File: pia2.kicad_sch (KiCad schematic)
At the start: 40 parts, among them IC25 LM393P, IC31 74LS02N, IC34 MC14050BCP, IC35 MC6821

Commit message: handle 27C512
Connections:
- net GND: no longer IC35.12 (PB2)
- new net MEM-SIZE: IC35.12 (PB2)
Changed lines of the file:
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@@
     )
   )
-  (global_label "GM2" (shape input) (at 74.93 87.122 0) (fields_autoplaced)
-    (effects (font (size 1.27 1.27)) (justify left))
-    (property "Intersheetrefs" "${INTERSHEET_REFS}" (at 81.1852 87.0426 0)
-      (effects (font (size 1.27 1.27)) (justify left) hide)
-    )
-  )
-  (global_label "GM1" (shape input) (at 74.93 84.582 0) (fields_autoplaced)
-    (effects (font (size 1.27 1.27)) (justify left))
-    (property "Intersheetrefs" "${INTERSHEET_REFS}" (at 81.1852 84.5026 0)
+  (global_label "GM2" (shape output) (at 74.93 87.122 0) (fields_autoplaced)
+    (effects (font (size 1.27 1.27)) (justify left))
+    (property "Intersheetrefs" "${INTERSHEET_REFS}" (at 81.1125 87.122 0)
+      (effects (font (size 1.27 1.27)) (justify left) hide)
+    )
+  )
+  (global_label "GM1" (shape output) (at 74.93 84.582 0) (fields_autoplaced)
+    (effects (font (size 1.27 1.27)) (justify left))
+    (property "Intersheetrefs" "${INTERSHEET_REFS}" (at 81.1125 84.582 0)
       (effects (font (size 1.27 1.27)) (justify left) hide)
     )
@@
     )
   )
-  (global_label "GM0" (shape input) (at 74.93 82.042 0) (fields_autoplaced)
-    (effects (font (size 1.27 1.27)) (justify left))
-    (property "Intersheetrefs" "${INTERSHEET_REFS}" (at 81.1852 81.9626 0)
+  (global_label "GM0" (shape output) (at 74.93 82.042 0) (fields_autoplaced)
+    (effects (font (size 1.27 1.27)) (justify left))
+    (property "Intersheetrefs" "${INTERSHEET_REFS}" (at 81.1125 82.042 0)
       (effects (font (size 1.27 1.27)) (justify left) hide)
     )
@@
     )
   )
-  (global_label "CSS" (shape input) (at 74.93 79.502 0) (fields_autoplaced)
-    (effects (font (size 1.27 1.27)) (justify left))
-    (property "Intersheetrefs" "${INTERSHEET_REFS}" (at 80.9432 79.4226 0)
+  (global_label "CSS" (shape output) (at 74.93 79.502 0) (fields_autoplaced)
+    (effects (font (size 1.27 1.27)) (justify left))
+    (property "Intersheetrefs" "${INTERSHEET_REFS}" (at 80.8706 79.502 0)
       (effects (font (size 1.27 1.27)) (justify left) hide)
     )
@@
     )
   )
-  (global_label "~{A}{slash}G" (shape input) (at 74.93 89.662 0) (fields_autoplaced)
-    (effects (font (size 1.27 1.27)) (justify left))
-    (property "Intersheetrefs" "${INTERSHEET_REFS}" (at 80.9432 89.5826 0)
+  (global_label "~{A}{slash}G" (shape output) (at 74.93 89.662 0) (fields_autoplaced)
+    (effects (font (size 1.27 1.27)) (justify left))
+    (property "Intersheetrefs" "${INTERSHEET_REFS}" (at 80.8707 89.662 0)
       (effects (font (size 1.27 1.27)) (justify left) hide)
     )
@@
     (property "Intersheetrefs" "${INTERSHEET_REFS}" (at 213.1404 49.4506 0)
       (effects (font (size 1.27 1.27)) (justify right) hide)
+    )
+  )
+  (global_label "MEM-SIZE" (shape output) (at 74.93 76.962 0) (fields_autoplaced)
+    (effects (font (size 1.27 1.27)) (justify left))
+    (property "Intersheetrefs" "${INTERSHEET_REFS}" (at 86.9786 76.962 0)
+      (effects (font (size 1.27 1.27)) (justify left) hide)
     )
   )
@@
         )
       )
-    )
-  )
-  (symbol (lib_id "power:GND") (at 74.93 76.962 90) (unit 1)
-    (in_bom yes) (on_board yes) (dnp no) (fields_autoplaced)
-    (property "Reference" "#PWR0229" (at 81.28 76.962 0)
-      (effects (font (size 1.27 1.27)) hide)
-    )
-    (property "Value" "GND" (at 78.74 77.597 90)
-      (effects (font (size 1.27 1.27)) (justify right))
-    )
-    (property "Footprint" "" (at 74.93 76.962 0)
-      (effects (font (size 1.27 1.27)) hide)
-    )
-    (property "Datasheet" "" (at 74.93 76.962 0)
-      (effects (font (size 1.27 1.27)) hide)
-    )
-    (pin "1")
-    (instances
-      (project "Dragon32"
-        (path "/0c3dceba-7c95-4b3d-b590-0eb581444beb/28dac1c2-804e-40fd-9ff5-acdb4226ab76"
-          (reference "#PWR0229") (unit 1)
-        )
-      )

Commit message: add control for pia 3
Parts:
- added C2: 10uF, Capacitor_THT:CP_Radial_D5.0mm_P2.50mm, symbol Device:C_Polarized_Small
- added IC9: MC6821, Package_DIP:DIP-40_W15.24mm, symbol Motorola PIA:MC6821
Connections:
- net +5V: now also C2.1, IC9.20 (VCC), IC9.22 (CS0), IC9.24 (CS1)
- net A0: now also IC9.36 (RS0)
- net A1: now also IC9.35 (RS1)
- net D0: now also IC9.33 (D0)
- net D1: now also IC9.32 (D1)
- net D2: now also IC9.31 (D2)
- net D3: now also IC9.30 (D3)
- net D4: now also IC9.29 (D4)
- net D5: now also IC9.28 (D5)
- net D6: now also IC9.27 (D6)
- net D7: now also IC9.26 (D7)
- net E: now also IC9.25 (E)
- net GND: now also C2.2, IC9.1 (VSS)
- net R/~{W}: now also IC9.21 (R/~{W})
- net ~{FIRQ}: now also IC9.37 (~{IRQB}), IC9.38 (~{IRQA})
- net ~{RES}: now also IC9.34 (~{RESET})
- net P1 renamed P1a
- new net P1b: IC9.23 (~{CS2})
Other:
- moved on the sheet: C26, C27, C35, C44, C48, D1, D2, D3, D7, IC25A, IC34, PL4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

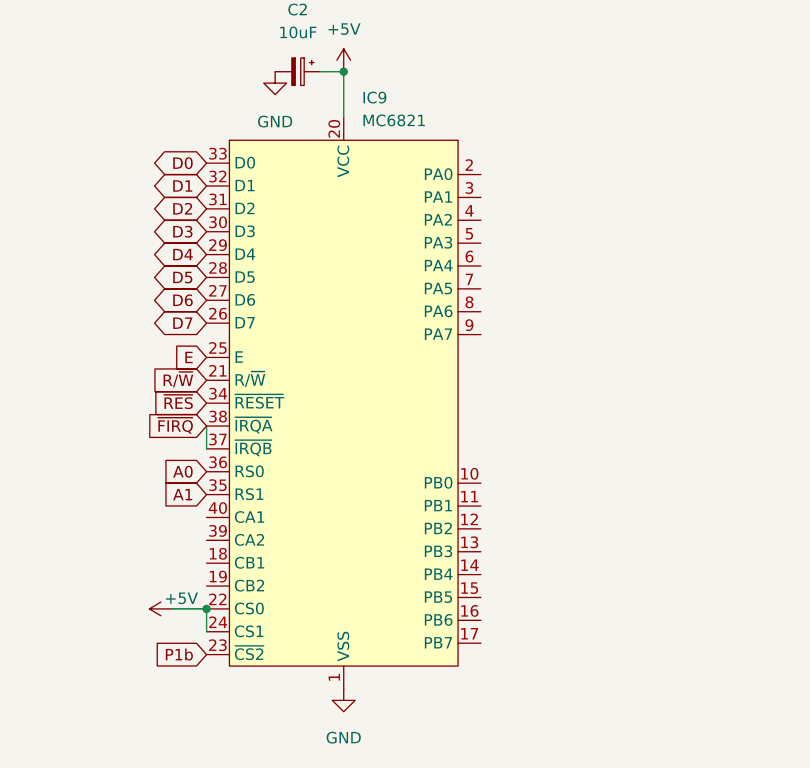
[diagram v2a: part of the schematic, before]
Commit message: complete tracing for fabrication
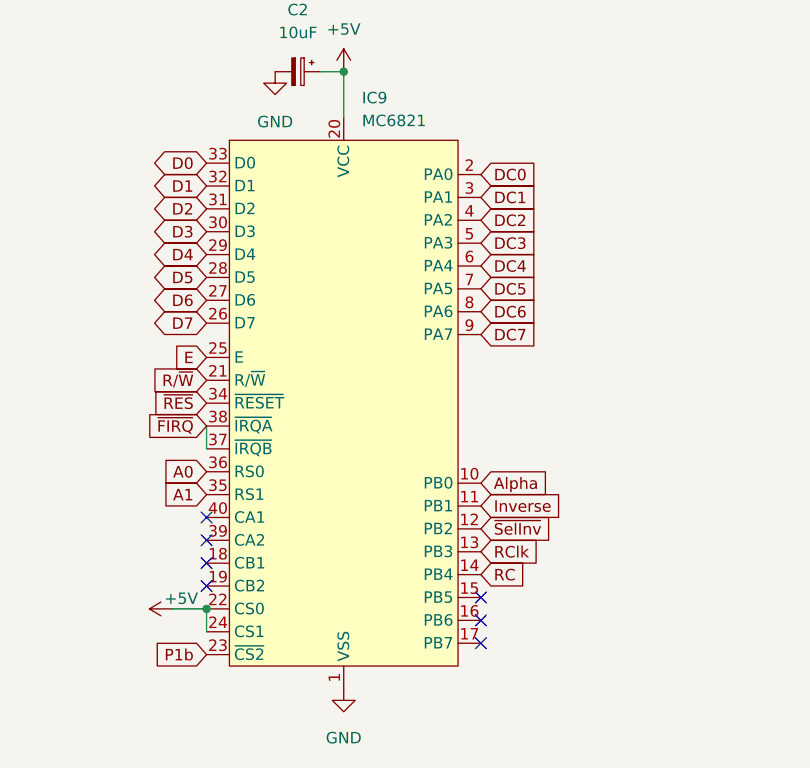
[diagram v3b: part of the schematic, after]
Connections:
- net Alpha: now reaches IC9.10 (PB0)
- net Inverse: now reaches IC9.11 (PB1)
- net ~{SelInv}: now reaches IC9.12 (PB2)
- net RClk: now reaches IC9.13 (PB3)
- net RC: now reaches IC9.14 (PB4)
- net DC0: now reaches IC9.2 (PA0)
- net DC1: now reaches IC9.3 (PA1)
- net DC2: now reaches IC9.4 (PA2)
- net DC3: now reaches IC9.5 (PA3)
- net DC4: now reaches IC9.6 (PA4)
- net DC5: now reaches IC9.7 (PA5)
- net DC6: now reaches IC9.8 (PA6)
- net DC7: now reaches IC9.9 (PA7)
- no-connect marks 1 -> 8
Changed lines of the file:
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@@
   (junction (at 44.45 85.852) (diameter 0) (color 0 0 0 0)
   )
+  (no_connect (at 74.93 170.18))
+  (no_connect (at 44.45 166.37))
+  (no_connect (at 44.45 161.29))
+  (no_connect (at 44.45 163.83))
+  (no_connect (at 44.45 168.91))
+  (no_connect (at 74.93 172.72))
   (no_connect (at 225.933 47.0903))
+  (no_connect (at 74.93 175.26))
   (wire (pts (xy 288.163 39.37) (xy 283.21 39.37))
     (stroke (width 0) (type default))
@@
     )
   )
+  (global_label "RClk" (shape input) (at 74.93 165.1 0) (fields_autoplaced)
+    (effects (font (size 1.27 1.27)) (justify left))
+    (property "Intersheetrefs" "${INTERSHEET_REFS}" (at 82.0691 165.1 0)
+      (effects (font (size 1.27 1.27)) (justify left) hide)
+    )
+  )
+  (global_label "Inverse" (shape input) (at 74.93 160.02 0) (fields_autoplaced)
+    (effects (font (size 1.27 1.27)) (justify left))
+    (property "Intersheetrefs" "${INTERSHEET_REFS}" (at 84.6281 160.02 0)
+      (effects (font (size 1.27 1.27)) (justify left) hide)
+    )
+  )
   (global_label "D3" (shape bidirectional) (at 44.45 43.942 180) (fields_autoplaced)
     (effects (font (size 1.27 1.27)) (justify right))
@@
     )
   )
+  (global_label "Alpha" (shape input) (at 74.93 157.48 0) (fields_autoplaced)
+    (effects (font (size 1.27 1.27)) (justify left))
+    (property "Intersheetrefs" "${INTERSHEET_REFS}" (at 83.116 157.48 0)
+      (effects (font (size 1.27 1.27)) (justify left) hide)
+    )
+  )
   (global_label "D0" (shape bidirectional) (at 44.45 36.322 180) (fields_autoplaced)
     (effects (font (size 1.27 1.27)) (justify right))
@@
     )
   )
+  (global_label "DC6" (shape input) (at 74.93 138.43 0) (fields_autoplaced)
+    (effects (font (size 1.27 1.27)) (justify left))
+    (property "Intersheetrefs" "${INTERSHEET_REFS}" (at 81.5853 138.43 0)
+      (effects (font (size 1.27 1.27)) (justify left) hide)
+    )
+  )
   (global_label "EAR" (shape input) (at 194.564 79.883 180) (fields_autoplaced)
     (effects (font (size 1.27 1.27)) (justify right))
@@
     )
   )
+  (global_label "RC" (shape input) (at 74.93 167.64 0) (fields_autoplaced)
+    (effects (font (size 1.27 1.27)) (justify left))
+    (property "Intersheetrefs" "${INTERSHEET_REFS}" (at 80.3758 167.64 0)
+      (effects (font (size 1.27 1.27)) (justify left) hide)
+    )
+  )
+  (global_label "DC4" (shape input) (at 74.93 133.35 0) (fields_autoplaced)
+    (effects (font (size 1.27 1.27)) (justify left))
+    (property "Intersheetrefs" "${INTERSHEET_REFS}" (at 81.5853 133.35 0)
+      (effects (font (size 1.27 1.27)) (justify left) hide)
+    )
+  )
   (global_label "P1b" (shape input) (at 44.45 176.53 180) (fields_autoplaced)
     (effects (font (size 1.27 1.27)) (justify right))
@@
     )
   )
+  (global_label "DC1" (shape input) (at 74.93 125.73 0) (fields_autoplaced)
+    (effects (font (size 1.27 1.27)) (justify left))
+    (property "Intersheetrefs" "${INTERSHEET_REFS}" (at 81.5853 125.73 0)
+      (effects (font (size 1.27 1.27)) (justify left) hide)
+    )
+  )
   (global_label "MIC" (shape output) (at 155.067 68.58 0) (fields_autoplaced)
     (effects (font (size 1.27 1.27)) (justify left))
@@
     )
   )
+  (global_label "~{SelInv}" (shape input) (at 74.93 162.56 0) (fields_autoplaced)
+    (effects (font (size 1.27 1.27)) (justify left))
+    (property "Intersheetrefs" "${INTERSHEET_REFS}" (at 83.5999 162.56 0)
+      (effects (font (size 1.27 1.27)) (justify left) hide)
+    )
+  )
+  (global_label "DC2" (shape input) (at 74.93 128.27 0) (fields_autoplaced)
+    (effects (font (size 1.27 1.27)) (justify left))
+    (property "Intersheetrefs" "${INTERSHEET_REFS}" (at 81.5853 128.27 0)
+      (effects (font (size 1.27 1.27)) (justify left) hide)
+    )
+  )
   (global_label "~{BUSY}" (shape bidirectional) (at 74.93 71.882 0) (fields_autoplaced)
     (effects (font (size 1.27 1.27)) (justify left))
@@
     )
   )
+  (global_label "DC7" (shape input) (at 74.93 140.97 0) (fields_autoplaced)
+    (effects (font (size 1.27 1.27)) (justify left))
+    (property "Intersheetrefs" "${INTERSHEET_REFS}" (at 81.5853 140.97 0)
+      (effects (font (size 1.27 1.27)) (justify left) hide)
+    )
+  )
   (global_label "~{ACK}" (shape output) (at 44.45 75.692 180) (fields_autoplaced)
     (effects (font (size 1.27 1.27)) (justify right))
@@
     )
   )
+  (global_label "DC5" (shape input) (at 74.93 135.89 0) (fields_autoplaced)
+    (effects (font (size 1.27 1.27)) (justify left))
+    (property "Intersheetrefs" "${INTERSHEET_REFS}" (at 81.5853 135.89 0)
+      (effects (font (size 1.27 1.27)) (justify left) hide)
+    )
+  )
   (global_label "PIADAC1" (shape input) (at 260.35 39.37 180) (fields_autoplaced)
     (effects (font (size 1.27 1.27)) (justify right))
@@
     )
   )
+  (global_label "DC0" (shape input) (at 74.93 123.19 0) (fields_autoplaced)
+    (effects (font (size 1.27 1.27)) (justify left))
+    (property "Intersheetrefs" "${INTERSHEET_REFS}" (at 81.5853 123.19 0)
+      (effects (font (size 1.27 1.27)) (justify left) hide)
+    )
+  )
   (global_label "PIADAC3" (shape output) (at 74.93 50.292 0) (fields_autoplaced)
     (effects (font (size 1.27 1.27)) (justify left))
@@
       (effects (font (size 1.27 1.27)) (justify left) hide)
     )
+  )
+  (global_label "DC3" (shape input) (at 74.93 130.81 0) (fields_autoplaced)
+    (effects (font (size 1.27 1.27)) (justify left))
+    (property "Intersheetrefs" "${INTERSHEET_REFS}" (at 81.5853 130.81 0)
+      (effects (font (size 1.27 1.27)) (justify left) hide)
+    )

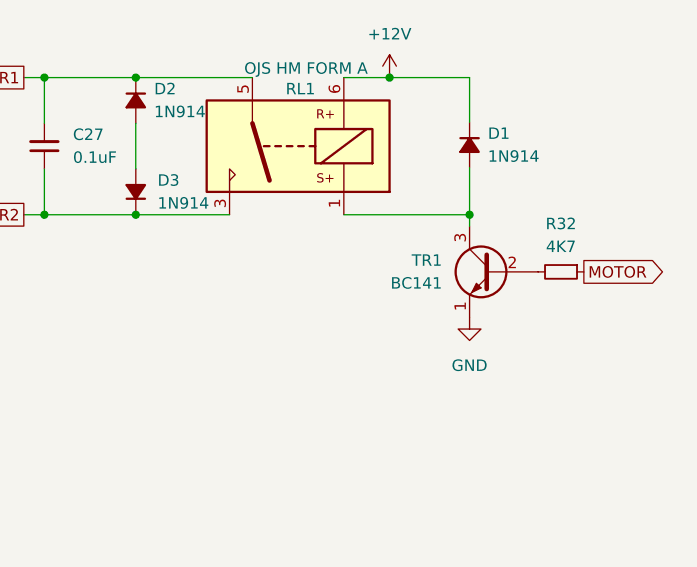
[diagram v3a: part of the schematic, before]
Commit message: fix rom and pia select traces
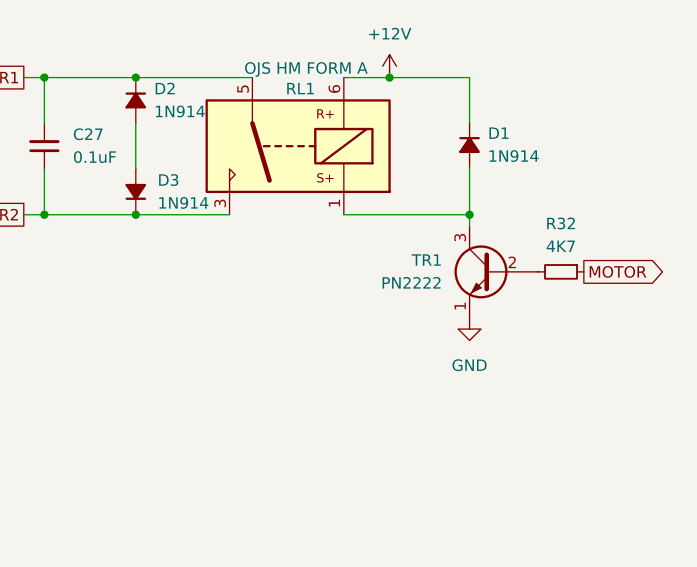
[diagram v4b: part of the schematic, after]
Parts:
- R32: footprint Resistor_THT:R_Axial_DIN0207_L6.3mm_D2.5mm_P10.16mm_Horizontal -> Resistor_THT:R_Axial_DIN0207_L6.3mm_D2.5mm_P2.54mm_Vertical
- TR1: value BC141 -> PN2222
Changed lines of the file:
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@@
       (effects (font (size 1.27 1.27)))
     )
-    (property "Footprint" "Resistor_THT:R_Axial_DIN0207_L6.3mm_D2.5mm_P10.16mm_Horizontal" (at 389.89 53.34 0)
+    (property "Footprint" "Resistor_THT:R_Axial_DIN0207_L6.3mm_D2.5mm_P2.54mm_Vertical" (at 389.89 53.34 0)
       (effects (font (size 1.27 1.27)) hide)
     )
@@
       (effects (font (size 1.27 1.27)) (justify left))
     )
-    (property "Value" "BC141" (at 376.682 54.6099 0)
+    (property "Value" "PN2222" (at 376.682 54.6099 0)
       (effects (font (size 1.27 1.27)) (justify left))
     )

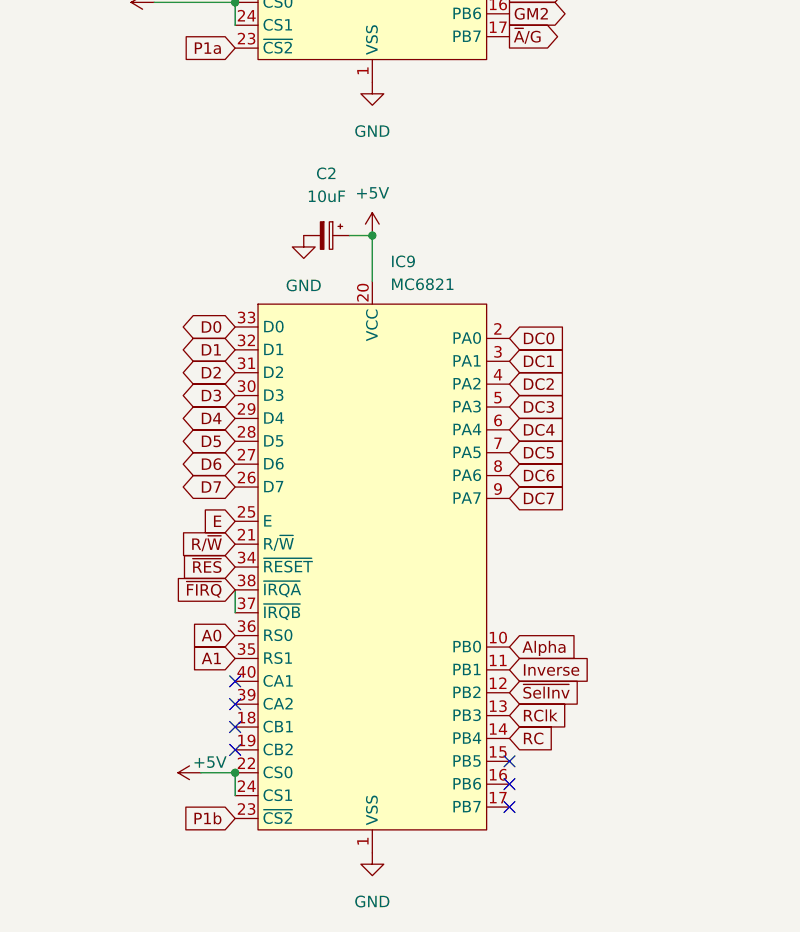
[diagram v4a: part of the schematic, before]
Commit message: reinforce power rails
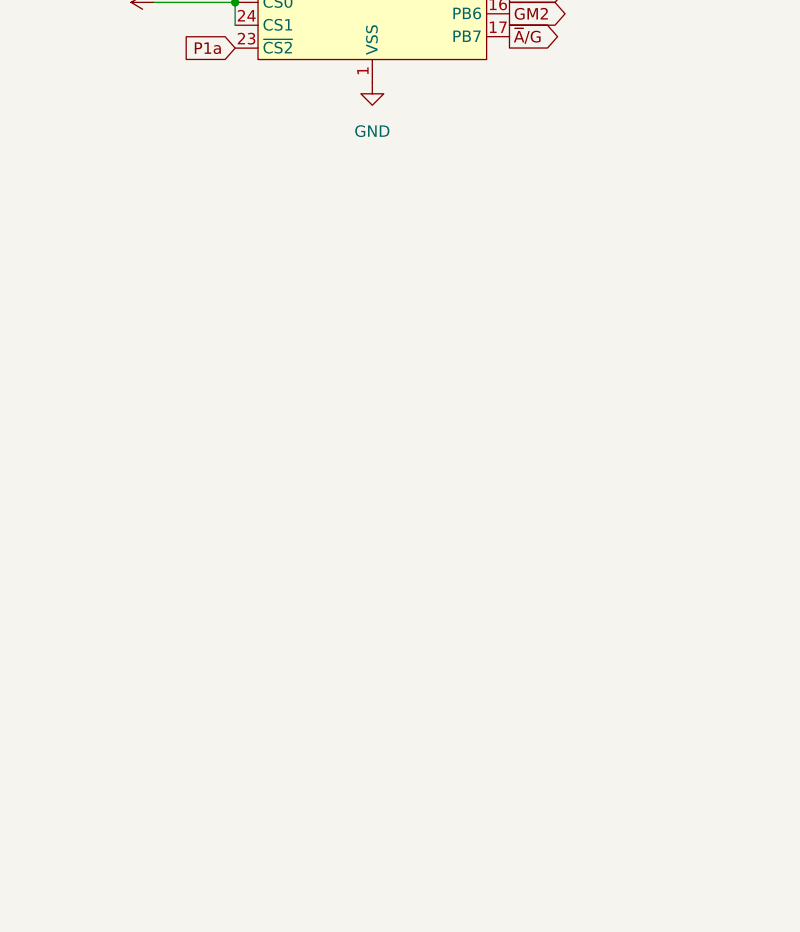
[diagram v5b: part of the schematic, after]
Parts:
- removed C2: 10uF, Capacitor_THT:CP_Radial_D5.0mm_P2.50mm, symbol Device:C_Polarized_Small
- removed IC9: MC6821, Package_DIP:DIP-40_W15.24mm, symbol Motorola PIA:MC6821
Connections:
- no-connect marks 8 -> 1

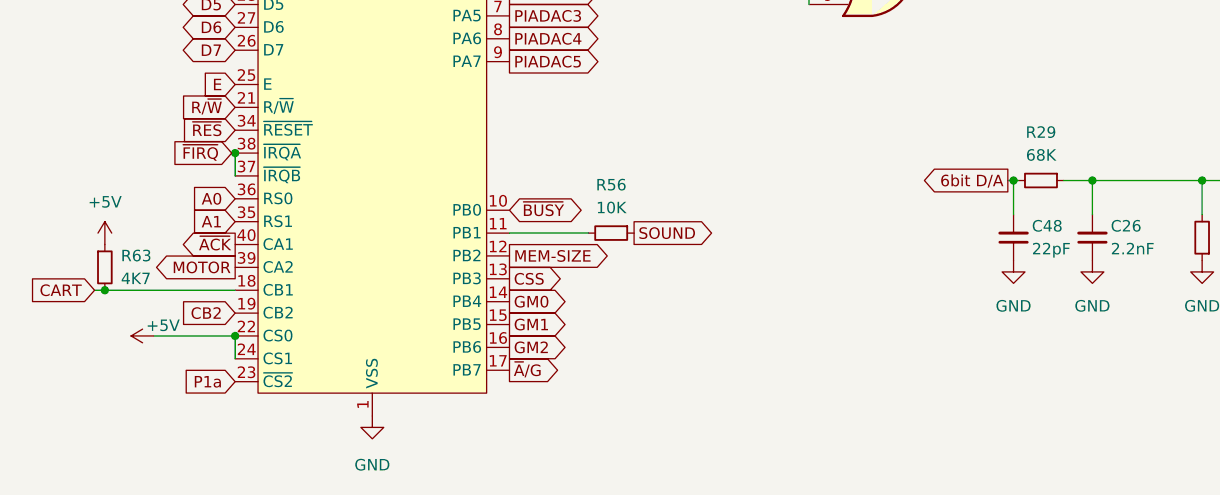
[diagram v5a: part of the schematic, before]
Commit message: reinforce audio traces
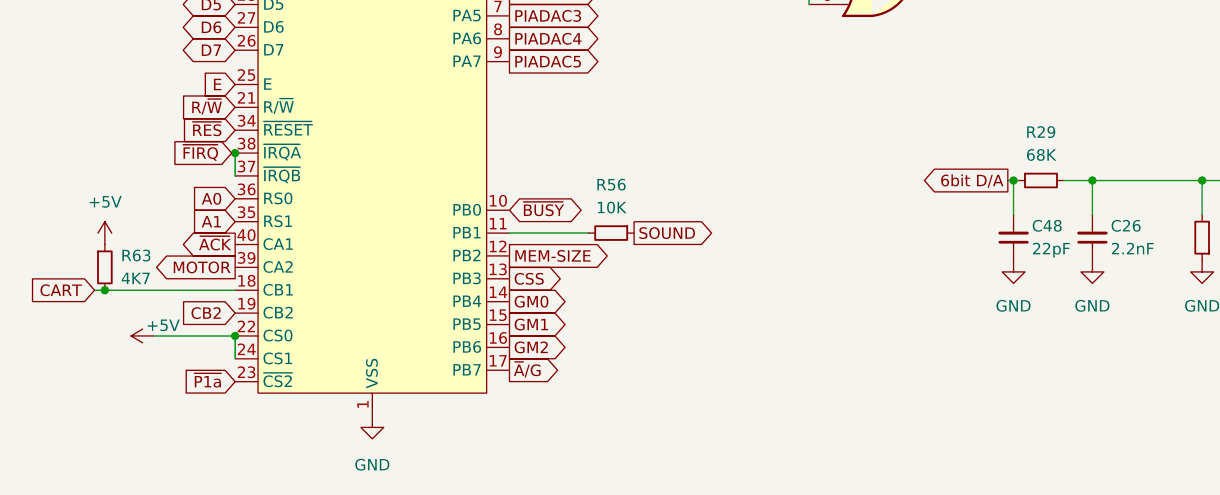
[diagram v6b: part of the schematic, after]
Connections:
- net 6bit D/A: now also R29.1; no longer R29.2
- net MIC: now also R29.2; no longer R29.1
- net P1a renamed ~{P1a}
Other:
- moved on the sheet: R29
